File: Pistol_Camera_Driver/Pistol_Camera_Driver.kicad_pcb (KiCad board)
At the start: 2 copper layers, 79.8 x 46.1 mm, 98 parts, among them J1 Screw_Terminal_01x02, J11 Screw_Terminal_01x02, J12 Screw_Terminal_01x02, J13 I2C, J14 Screw_Terminal_01x02, J15 Screw_Terminal_01x02, J16 Screw_Terminal_01x02, J17 Screw_Terminal_01x02, J18 Screw_Terminal_01x02, J19 I2C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

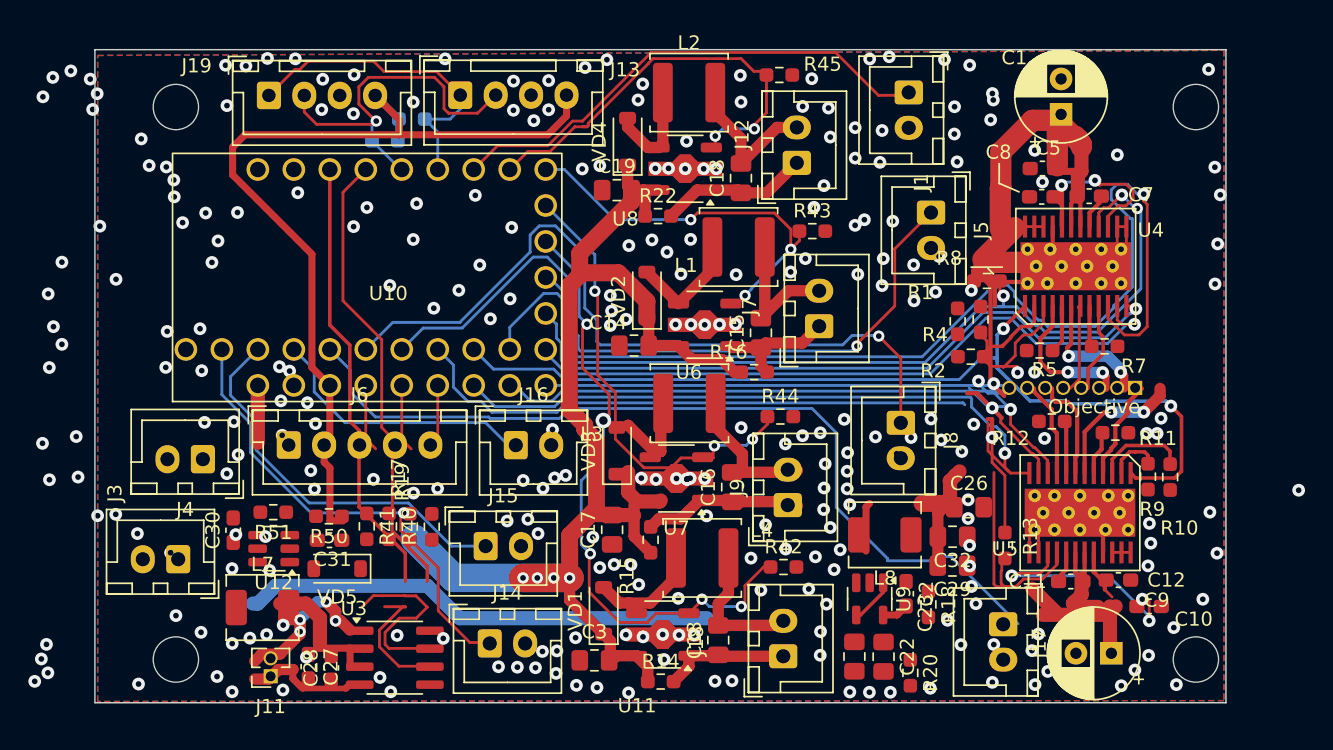
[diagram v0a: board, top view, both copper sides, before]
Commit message: v1.0 Draft routing and DRC completed
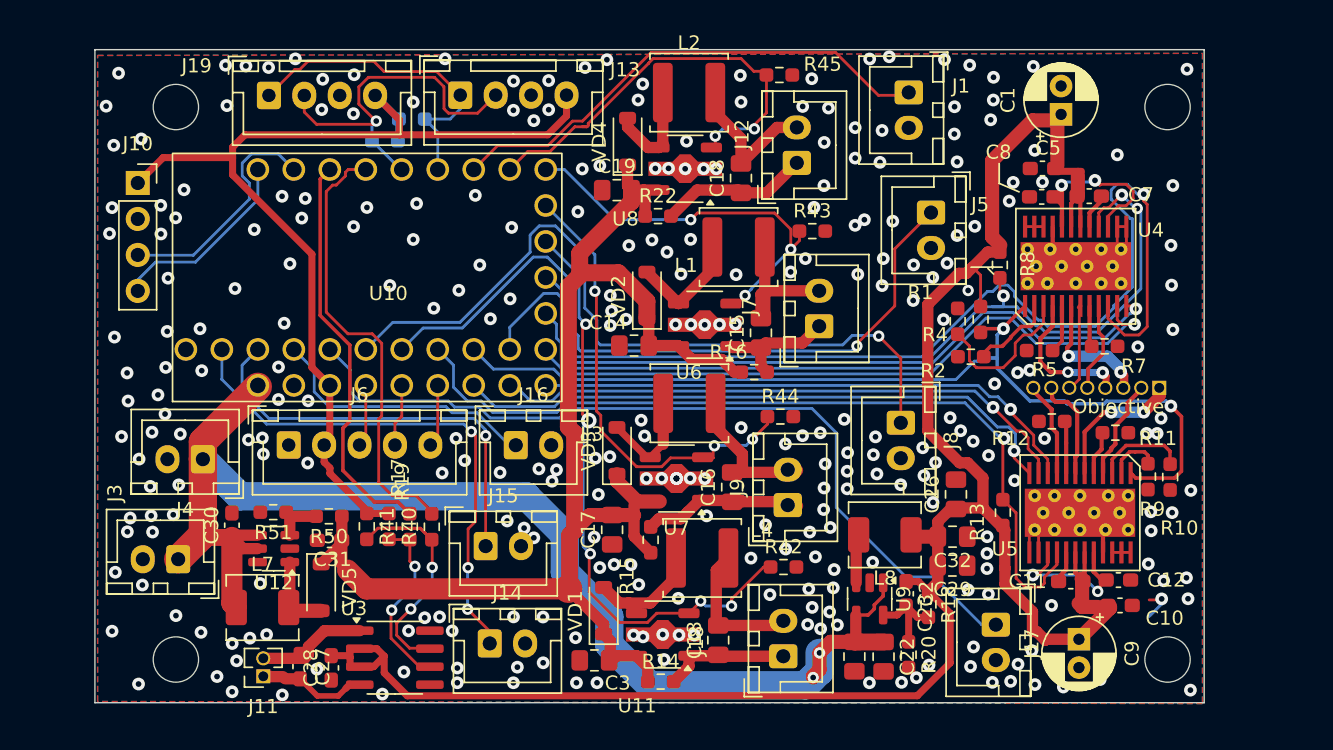
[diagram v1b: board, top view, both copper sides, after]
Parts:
- added J10: I2C, Connector_PinSocket_2.54mm:PinSocket_1x04_P2.54mm_Vertical, F.Cu at (38.0, 41.0)
- C1, C9: footprint Capacitor_THT:CP_Radial_D6.3mm_P2.50mm -> Capacitor_THT:CP_Radial_D5.0mm_P2.00mm
- U9: value ~ -> RY3430
- moved C9 2.49 mm to (104.4, 73.2), turned to -90 degrees
- moved R13 2.33 mm to (99.0, 64.3), turned to 90 degrees
- moved C10 2.05 mm to (107.3, 70.8)
- moved REF** 2.00 mm to (110.6, 35.6)
- moved REF** 2.00 mm to (110.6, 74.7)
- moved VD5 1.74 mm to (50.9, 69.6), turned to -90 degrees
- moved J2 1.70 mm to (110.1, 55.5)
- moved R8 1.45 mm to (98.8, 46.8), turned to -90 degrees
- moved C26 1.29 mm to (95.7, 63.0), turned to 90 degrees
- moved R20 1.29 mm to (92.4, 74.3)
- moved C27 0.58 mm to (49.4, 75.2)
- moved J17 0.52 mm to (98.5, 72.2)
- moved J11 0.52 mm to (46.8, 75.8)
- moved C30 0.36 mm to (44.6, 65.2)
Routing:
- net VBUS: track 7.26 -> 95.7 mm, vias 0 -> 2
- net +3.3VP: track 100.3 -> 145.0 mm, vias 1 -> 0
- net (no net): track 33.5 -> 0.00 mm
- net TX: track 0.00 -> 16.6 mm
- net RX: track 0.00 -> 13.7 mm
- net +3V3: track 63.9 -> 72.4 mm
- net Net-(U3-IB): track 12.4 -> 18.9 mm, vias 0 -> 2
- net VPP: track 92.3 -> 98.2 mm, vias 4 -> 0
- net Net-(U12-SW): track 0.00 -> 5.62 mm
- net Net-(J11-Pin_2): track 12.7 -> 7.93 mm, vias 4 -> 0
- net Net-(U9-FB): track 1.88 -> 6.39 mm
- net K6: track 33.0 -> 37.2 mm, vias 1 -> 3
- net Net-(U12-FB): track 0.00 -> 3.95 mm
- net nEN2: track 42.8 -> 39.1 mm
- net Net-(U3-IA): track 8.77 -> 12.3 mm, vias 0 -> 2
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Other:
- board size 79.8 x 46.1 mm -> 78.3 x 46.1 mm
